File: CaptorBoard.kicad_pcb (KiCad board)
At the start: 2 copper layers, 86 x 68.5 mm, 55 parts, among them CON1 MINI-USB-SHELD-MC32598, P1 Prog, P2 POWER, P3 EXT, Q1 IRLM6402TRPBF, SW1 CST06S08H, U1 PIC32MX795F512H-80I-PT, U2 MRF24J40MA-I-RM, U3 HTU21, U4 MPL115A2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

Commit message: Replace Value 550 ohm to 560ohm (mormailsition)
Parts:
- R12, R13: value 550R -> 560R

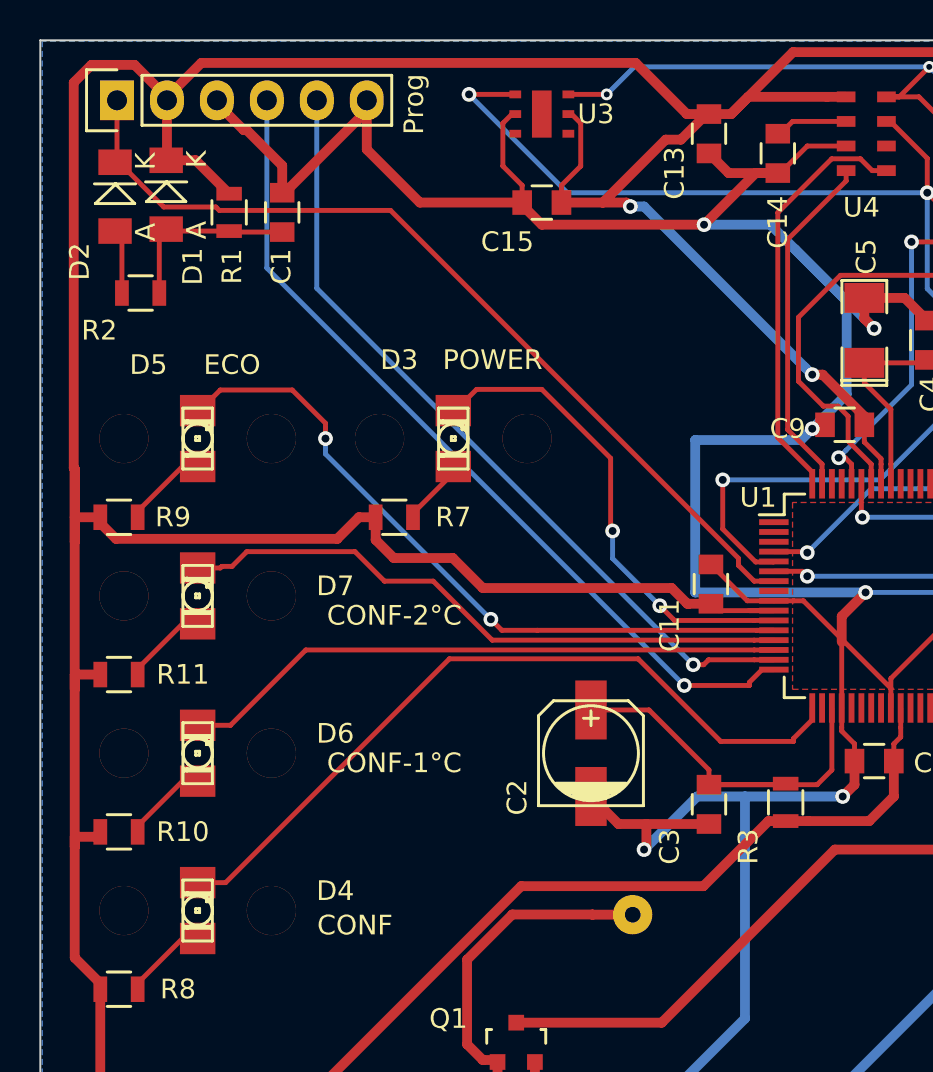
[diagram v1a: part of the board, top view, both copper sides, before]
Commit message: Change led package to 3mm
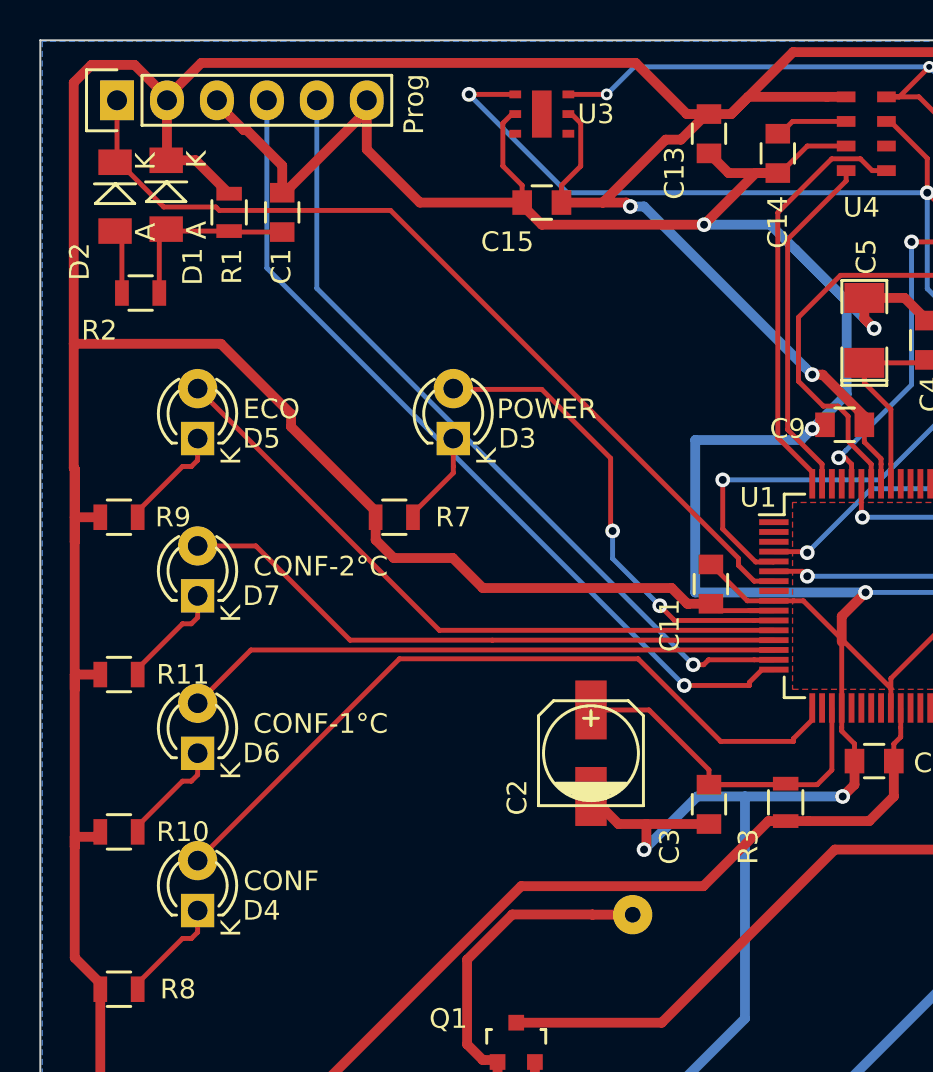
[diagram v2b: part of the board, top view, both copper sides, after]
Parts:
- D3, D4, D5, D6, D7: footprint pfo:LED-1206-Guide -> LEDs:LED-3MM
- U5: value VTX-214-003-105 -> VTX-214-005-005
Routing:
- net +3V3: track 371.2 -> 375.9 mm
- net Net-(D3-Pad1): track 3.43 -> 4.85 mm
- net /ECO: track 35.7 -> 34.4 mm, vias 2 -> 0
- net Net-(D7-Pad1): track 4.29 -> 5.53 mm
- net Net-(D6-Pad1): track 4.29 -> 5.53 mm
- net Net-(D5-Pad1): track 4.29 -> 5.53 mm
- net Net-(D4-Pad1): track 4.29 -> 5.53 mm

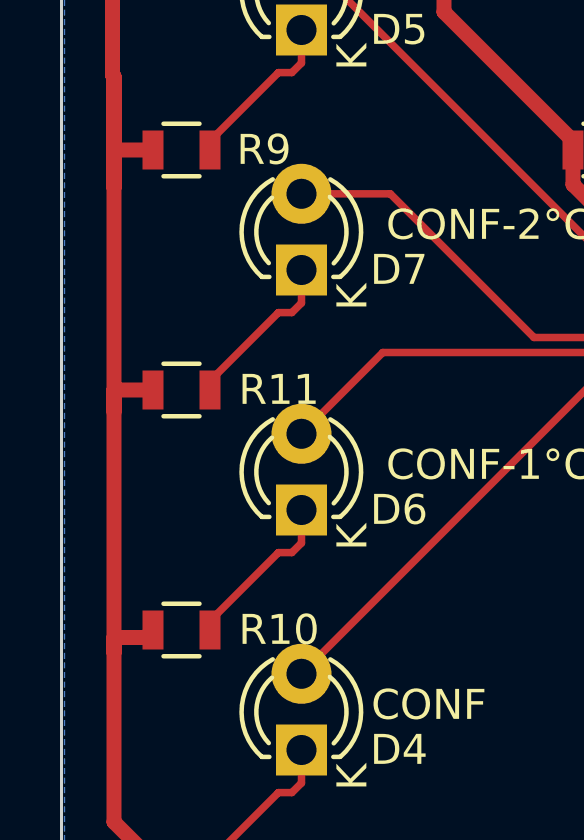
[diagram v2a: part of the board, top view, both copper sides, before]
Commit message: Change RH/temp sensor to STH21
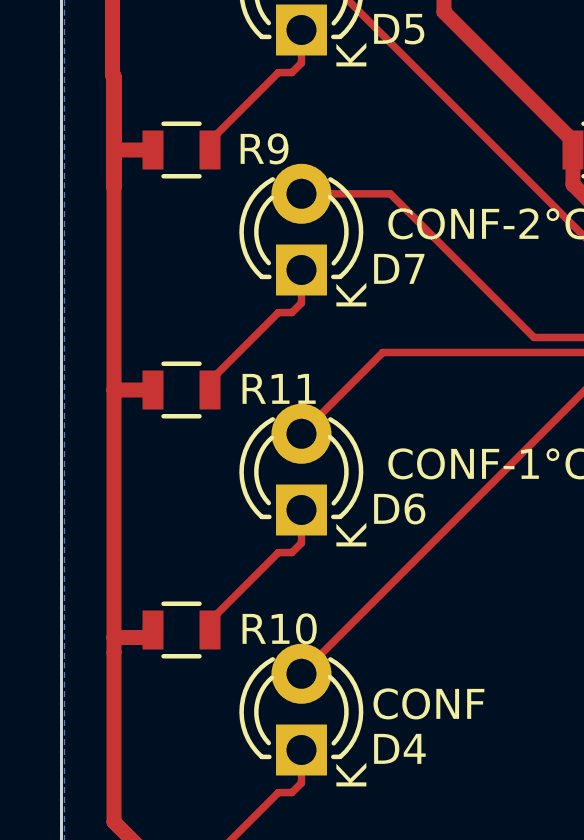
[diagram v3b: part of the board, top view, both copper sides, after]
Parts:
- U3: value HTU21 -> SHT25
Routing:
- net +3V3: track 375.9 -> 374.7 mm

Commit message: Change Button ref
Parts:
- SW1: value CST06S08H -> SKHHLVA010

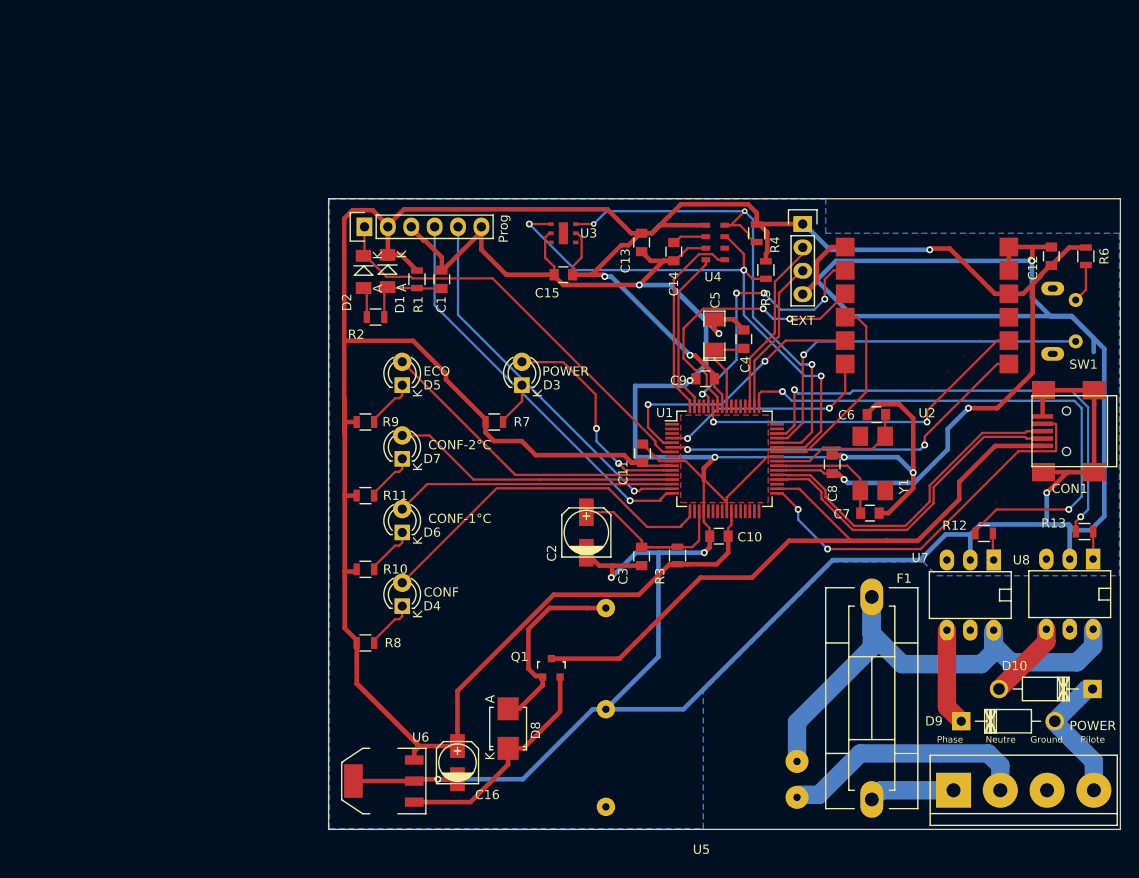
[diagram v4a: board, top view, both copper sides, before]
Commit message: finally use WeMos Mini
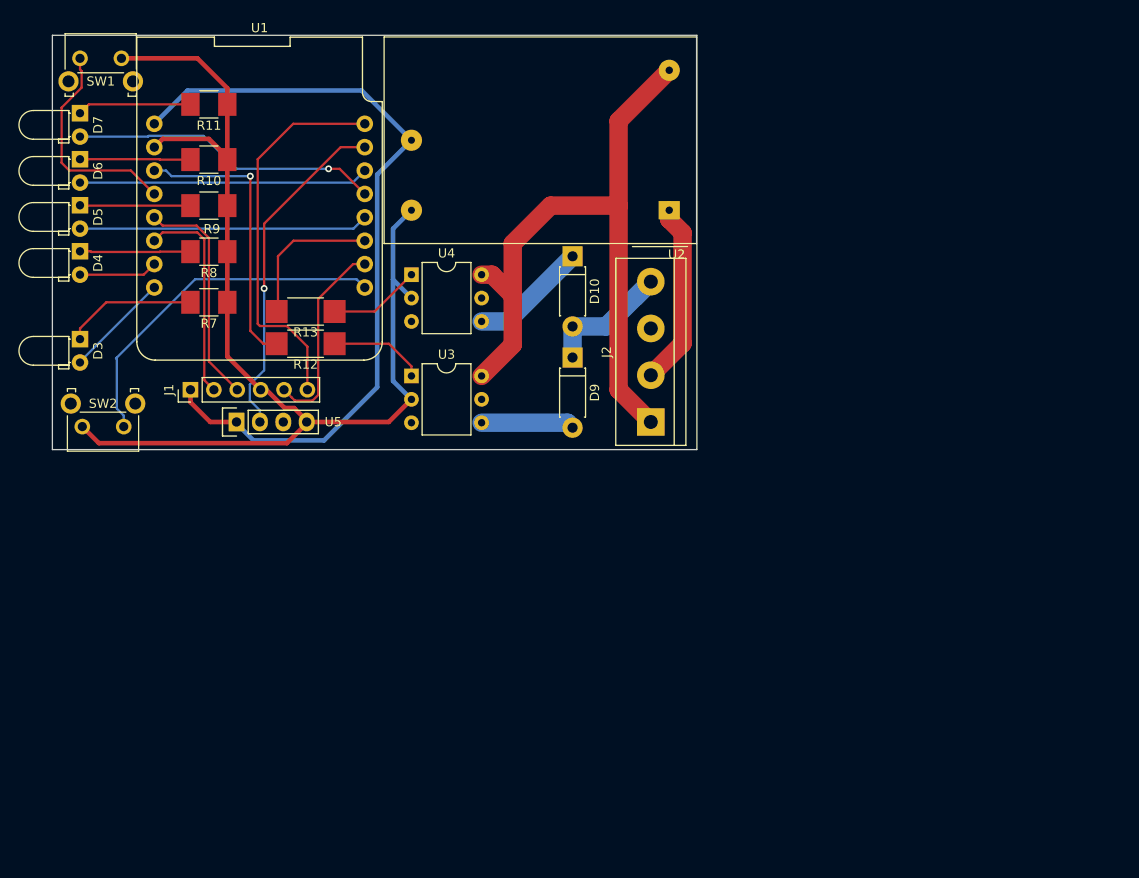
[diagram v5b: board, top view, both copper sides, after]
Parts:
- removed C1, C10, C11, C12, C13, C15, C3, C4, C8, C9: 100nF, Capacitors_SMD:C_0805
- removed C14: 1uF, Capacitors_SMD:C_0805
- removed C16: 1uF, Capacitors_SMD:c_elec_4x5.3
- removed C2: 10uF, Capacitors_SMD:c_elec_5x5.3
- removed C5: TPSA106K010R0900, SMD_Packages:SMD-1206_Pol
- removed C6, C7: 20pF, Capacitors_SMD:C_0805
- removed CON1: MINI-USB-SHELD-MC32598, pfo:USB_Mini-B
- removed D1, D2: BAS32L, Diodes_SMD:Diode-MiniMELF_Standard
- removed D8: B340A-E3/61T, Diodes_SMD:Diode-SMB_Standard
- removed F1: F_Small, Fuse_Holders_and_Fuses:Fuseholder5x20_horiz_SemiClosed_Casing10x25mm
- removed P1: Prog, Pin_Headers:Pin_Header_Straight_1x06
- removed P2: POWER, Connect:bornier4
- removed P3: EXT, Pin_Headers:Pin_Header_Straight_1x04
- removed Q1: IRLM6402TRPBF, Housings_SOT-23_SOT-143_TSOT-6:SOT-23
- removed R1: 68k, Resistors_SMD:R_0805
- removed R2, R6: 1k, Resistors_SMD:R_0805
- removed R3: 10R, Resistors_SMD:R_0805
- removed R4, R5: 2.2k, Resistors_SMD:R_0805
- removed U6: TC1262-3.3VDB, SMD_Packages:SOT-223
- removed U7, U8: MOC3042M, Housings_DIP:DIP-6__300_ELL
- removed Y1: FQ7050B-8.000, pfo:SMD_Crystal_FQ7050_Series
- added J1: Conn_01x06, Pin_Headers:Pin_Header_Straight_1x06_Pitch2.54mm, F.Cu at (85.0, 93.5)
- added J2: Screw_Terminal_01x04, Connectors_Terminal_Blocks:TerminalBlock_bornier-4_P5.08mm, F.Cu at (135.0, 97.0)
- added SW2: SKHHLVA010, Buttons_Switches_THT:SW_Tactile_SKHH_Angled, F.Cu at (77.8, 97.5)
- D10, D9: footprint Diodes_ThroughHole:Diode_DO-41_SOD81_Horizontal_RM10 -> Diodes_THT:D_DO-41_SOD81_P7.62mm_Horizontal
- D3, D4, D5, D6, D7: footprint LEDs:LED-3MM -> LEDs:LED_D3.0mm_Horizontal_O1.27mm_Z2.0mm
- R10, R11, R7, R8, R9: footprint Resistors_SMD:R_0805 -> Resistors_SMD:R_1210_HandSoldering
- R12, R13: footprint Resistors_SMD:R_0805 -> Resistors_SMD:R_2010_HandSoldering
- SW1: footprint pfo:CST06S -> Buttons_Switches_THT:SW_Tactile_SKHH_Angled
- U1: value PIC32MX795F512H-80I-PT -> WeMos_mini; footprint Housings_QFP:TQFP-64_10x10mm_Pitch0.5mm -> wemos-d1-mini:wemos-d1-mini-with-pin-header-and-connector
- U2: value MRF24J40MA-I-RM -> IRM-02-5; footprint pfo:MRF24J40MA -> Converters_DCDC_ACDC:ACDC-Conv_THTMeanWell-IRM-02-XX
- U3: value SHT25 -> MOC3041M; footprint pfo:HTU21 -> Housings_DIP:DIP-6_W7.62mm
- U4: value MPL115A2 -> MOC3041M; footprint pfo:MPL115A2 -> Housings_DIP:DIP-6_W7.62mm
- U5: value VTX-214-005-005 -> DHT22; footprint pfo:VTX-214-005-x -> pfo:DHT22_Temperature_Humidity
- moved SW1 111.2 mm to (73.0, 57.5), turned to 0 degrees
- moved R13 87.9 mm to (97.5, 85.0)
- moved R12 76.5 mm to (97.5, 88.5)
- moved D10 69.6 mm to (126.5, 79.0), turned to 270 degrees
- moved D9 61.6 mm to (126.5, 90.0), turned to 270 degrees
- moved U1 57.5 mm to (92.5, 73.5), turned to 270 degrees
- moved U5 56.2 mm to (93.8, 97.0)
- moved D6 53.6 mm to (73.0, 68.5), turned to 270 degrees
- moved D4 52.1 mm to (73.0, 78.5), turned to 270 degrees
- moved D7 51.3 mm to (73.0, 63.5), turned to 270 degrees
- moved D3 48.3 mm to (73.0, 88.0), turned to 270 degrees
- moved R10 47.6 mm to (87.0, 68.5), turned to 180 degrees
- moved R11 45.8 mm to (87.0, 62.5), turned to 180 degrees
- moved R8 45.8 mm to (87.0, 78.5), turned to 180 degrees
- moved D5 40.1 mm to (73.0, 73.5), turned to 270 degrees
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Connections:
- R10 pad 1: +3V3 -> GND
- R11 pad 1: +3V3 -> GND
- R7 pad 1: +3V3 -> GND
- R8 pad 1: +3V3 -> GND
- R9 pad 1: +3V3 -> GND
- SW1 pad 2: Net-(R6-Pad2) -> GND
- U1 pad 1: (no net) -> +5V
- U1 pad 10: +3V3 -> /ANA
- U1 pad 11: /POWER -> /PILOT_2
- U1 pad 15: /PGC -> /CAPTOR
- U1 pad 16: /PGD -> +3V3
- U1 pad 2: (no net) -> GND
- U1 pad 3: (no net) -> /PILOT_1
- U1 pad 4: /SCK_RF -> /SELECT
- U1 pad 5: /SDI_RF -> /SDA_EXT
- U1 pad 6: /SDO_RF -> /SCL_EXT
- U1 pad 7: /*MCLR -> /CONF
- U1 pad 8: (no net) -> /POWER
- U1 pad 9: GND -> /RESET
- U2 pad 1: GND -> /Neutre
- U2 pad 2: /RST_RF -> /Phase
- U2 pad 3: /WK_RF -> GND
- U2 pad 4: /INT_RF -> +5V
- U3 pad 1: /SDA_CAP -> Net-(R12-Pad1)
- U3 pad 4: (no net) -> Net-(D9-Pad2)
- U3 pad 5: +3V3 -> (no net)
- U3 pad 6: /SCL_CAP -> /Phase
- U4 pad 1: +3V3 -> Net-(R13-Pad1)
- U4 pad 2: Net-(C14-Pad1) -> GND
- U4 pad 3: GND -> (no net)
- U4 pad 4: /SHD_PRES -> Net-(D10-Pad1)
- U4 pad 5: /RST_PRES -> (no net)
- U4 pad 6: (no net) -> /Phase
- U5 pad 1: /Neutre -> +5V
- U5 pad 2: /Phase_F -> /CAPTOR
- U5 pad 3: /5V_SEC -> (no net)
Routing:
- net +3V3: track 374.7 -> 42.2 mm, vias 5 -> 0
- net GND: track 457.5 -> 126.8 mm, vias 11 -> 0
- net /VUSB: track 75.0 -> 0.00 mm
- net /Phase: track 9.29 -> 75.2 mm
- net /SDA_CAP: track 62.7 -> 0.00 mm, vias 3 -> 0
- net +5V: track 24.7 -> 85.9 mm
- net /Phase_F: track 58.5 -> 0.00 mm
- net /SCL_CAP: track 58.2 -> 0.00 mm, vias 3 -> 0
- net /*MCLR: track 45.7 -> 0.00 mm
- net /PGD: track 43.5 -> 0.00 mm, vias 1 -> 0
- net /USBID: track 42.3 -> 0.00 mm, vias 2 -> 0
- net /SDO_RF: track 41.1 -> 0.00 mm, vias 2 -> 0
- net /PGC: track 40.8 -> 0.00 mm, vias 1 -> 0
- net /RESET: track 0.00 -> 38.8 mm
- net /CS_RF: track 38.2 -> 0.00 mm, vias 2 -> 0
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- removed copper zone on B.Cu, net GND
- removed copper zone on F.Cu, net GND
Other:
- board size 86 x 68.5 mm -> 70 x 45 mm
- net class SPI removed
- net class USB data removed
- board text added: "-1°C"
- board text added: "-2°C"
- board text added: "1 - +5V 2 - SCL 3 - SDA 4 - GND 5 - ANA 6 - +3.3V"
- board text added: "Conf"
- board text added: "ECO"
- board text added: "Reset"
- board text added: "Select"
- board text added: "Status"
- board text added: "Terre"
- board text removed: "Ground"

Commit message: Board final
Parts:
- added F1: Fuse_Small, Fuse:Fuseholder_Littelfuse_Nano2_157x, F.Cu at (128.0, 83.5)
- D3, D4, D5, D6, D7: footprint LEDs:LED_D3.0mm_Horizontal_O1.27mm_Z2.0mm -> LEDs:LED_D3.0mm
- J2: value Screw_Terminal_01x04 -> MKDSN 1,5/ 4-5,08; footprint Connectors_Terminal_Blocks:TerminalBlock_bornier-4_P5.08mm -> TerminalBlocks_Phoenix:TerminalBlock_Phoenix_MKDS1.5-4pol
- R12, R13: footprint Resistors_SMD:R_2010_HandSoldering -> Resistors_SMD:R_1210_HandSoldering
- U3, U4: value MOC3041M -> MOC3040X
- moved SW2 44.6 mm to (98.5, 58.0), turned to 0 degrees
- moved R9 12.4 mm to (99.0, 70.5), turned to 270 degrees
- moved D6 11.3 mm to (77.0, 79.0)
- moved D3 11.0 mm to (81.0, 95.5), turned to 180 degrees
- moved R11 11.0 mm to (94.5, 70.5), turned to 270 degrees
- moved D5 10.9 mm to (77.5, 63.5)
- moved D4 8.94 mm to (77.0, 86.5)
- moved D7 8.54 mm to (77.0, 71.0)
- moved R10 7.91 mm to (89.5, 76.0), turned to 270 degrees
- moved SW1 7.50 mm to (80.5, 57.5)
- moved R12 5.59 mm to (103.0, 89.5)
- moved R13 5.59 mm to (103.0, 86.0)
- moved R7 5.32 mm to (83.5, 88.0), turned to 0 degrees
- moved D9 3.04 mm to (123.5, 90.5)
- moved D10 3.00 mm to (123.5, 79.0)
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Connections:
- D10 pad 2: /Pilote -> /CMD2
- D3 pad 2: /POWER -> GND
- D4 pad 2: /CONF -> GND
- D5 pad 2: /ECO -> GND
- D6 pad 2: /CONF-1°C -> GND
- D7 pad 2: /CONF-2°C -> GND
- D9 pad 1: /Pilote -> /CMD2
- J2 pad 1: /Phase -> (no net)
- J2 pad 2: /Neutre -> /CMD2
- J2 pad 3: (no net) -> Net-(F1-Pad2)
- J2 pad 4: /Pilote -> /Neutre
- R10 pad 1: GND -> Net-(D6-Pad1)
- R10 pad 2: Net-(D6-Pad1) -> /CONF-1°C
- R11 pad 1: GND -> Net-(D7-Pad1)
- R11 pad 2: Net-(D7-Pad1) -> /CONF-2°C
- R7 pad 1: GND -> Net-(D3-Pad1)
- R7 pad 2: Net-(D3-Pad1) -> /POWER
- R8 pad 1: GND -> Net-(D4-Pad1)
- R8 pad 2: Net-(D4-Pad1) -> /CONF
- R9 pad 1: GND -> Net-(D5-Pad1)
- R9 pad 2: Net-(D5-Pad1) -> /ECO
- U1 pad 12: /ECO -> /CONF-1°C
- U1 pad 13: /CONF-2°C -> /ECO
- U1 pad 14: /CONF-1°C -> /CAPTOR
- U1 pad 15: /CAPTOR -> /CONF-2°C
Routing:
- net /ECO: track 31.4 -> 5.04 mm
- net /CONF-2°C: track 33.6 -> 12.4 mm, vias 1 -> 0
- net /Phase: track 75.2 -> 57.4 mm
- net /CMD2: track 0.00 -> 17.0 mm
- net /Pilote: track 16.4 -> 0.00 mm
- net /CONF-1°C: track 31.5 -> 15.8 mm
- net Net-(D5-Pad1): track 12.0 -> 23.6 mm
- net /Neutre: track 19.9 -> 9.12 mm
- net /RESET: track 38.8 -> 28.4 mm
- net +3V3: track 42.2 -> 32.5 mm
- net Net-(F1-Pad2): track 0.00 -> 7.71 mm
- net /PILOT_2: track 16.2 -> 9.65 mm
- net Net-(D3-Pad1): track 14.3 -> 7.81 mm
- net Net-(D7-Pad1): track 12.4 -> 18.5 mm
- net /SELECT: track 23.8 -> 17.7 mm, vias 0 -> 1
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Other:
- board size 70 x 45 mm -> 65 x 45 mm
- net class Sector: clearance 0.5 -> 0.7
- board text added: "1 - +5V 2 - CAPTEUR 3 - NC 4 - GND"
- board text added: "1 - Terre 2 - Pilote 3 - Phase 4 - Neutre"
- board text removed: "Neutre"
- board text removed: "Phase"
- board text removed: "Pilote"
- board text removed: "Terre"

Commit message: new kicad version
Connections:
- net Net-(D10-Pad1) renamed /P2
- net Net-(D9-Pad2) renamed /P1
- net Net-(F1-Pad2) renamed /Phase_in
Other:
- net class Default removed
- net class I2C removed
- net class Power removed
- net class Sector removed
